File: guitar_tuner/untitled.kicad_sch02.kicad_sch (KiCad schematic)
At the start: 3 parts, among them Q2 NPN

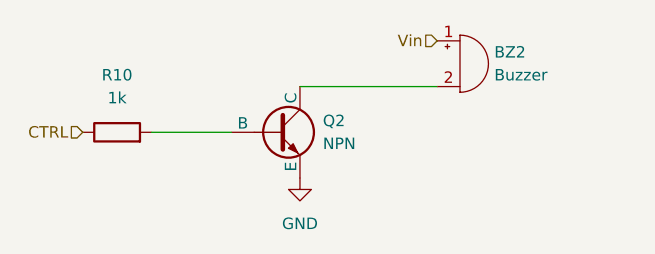
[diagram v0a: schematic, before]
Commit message: Buzzer Circuit Footprints and New Diode
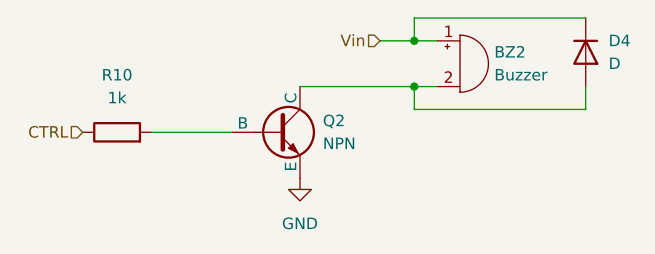
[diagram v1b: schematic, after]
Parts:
- added D4: D, Diode_SMD:D_0805_2012Metric_Pad1.15x1.40mm_HandSolder, symbol Device:D
- BZ2: footprint (none) -> Buzzer_Beeper:Buzzer_12x9.5RM7.6
- Q2: footprint (none) -> Package_TO_SOT_SMD:SOT-23_Handsoldering
- R10: footprint (none) -> Resistor_SMD:R_0805_2012Metric_Pad1.20x1.40mm_HandSolder
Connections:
- net Vin: now also D4.1 (K)
- net at BZ2.2 (-), Q2.1 (C): now also D4.2 (A)
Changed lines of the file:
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@@
 	(generator_version "9.0")
 	(paper "A4")
+	(junction
+		(at 157.48 99.06)
+		(diameter 0)
+		(color 0 0 0 0)
+	)
+	(junction
+		(at 157.48 93.98)
+		(diameter 0)
+		(color 0 0 0 0)
+	)
+	(wire
+		(pts
+			(xy 157.48 99.06) (xy 160.02 99.06)
+		)
+		(stroke
+			(width 0)
+			(type default)
+		)
+	)
+	(wire
+		(pts
+			(xy 176.53 101.6) (xy 176.53 99.06)
+		)
+		(stroke
+			(width 0)
+			(type default)
+		)
+	)
+	(wire
+		(pts
+			(xy 157.48 93.98) (xy 160.02 93.98)
+		)
+		(stroke
+			(width 0)
+			(type default)
+		)
+	)
 	(wire
 		(pts
@@
 	(wire
 		(pts
-			(xy 144.78 99.06) (xy 160.02 99.06)
+			(xy 144.78 99.06) (xy 157.48 99.06)
+		)
+		(stroke
+			(width 0)
+			(type default)
+		)
+	)
+	(wire
+		(pts
+			(xy 157.48 93.98) (xy 157.48 91.44)
+		)
+		(stroke
+			(width 0)
+			(type default)
+		)
+	)
+	(wire
+		(pts
+			(xy 157.48 101.6) (xy 176.53 101.6)
+		)
+		(stroke
+			(width 0)
+			(type default)
+		)
+	)
+	(wire
+		(pts
+			(xy 157.48 91.44) (xy 176.53 91.44)
+		)
+		(stroke
+			(width 0)
+			(type default)
+		)
+	)
+	(wire
+		(pts
+			(xy 153.67 93.98) (xy 157.48 93.98)
+		)
+		(stroke
+			(width 0)
+			(type default)
+		)
+	)
+	(wire
+		(pts
+			(xy 157.48 99.06) (xy 157.48 101.6)
 		)
 		(stroke
@@
 	(hierarchical_label "Vin"
 		(shape input)
-		(at 160.02 93.98 180)
+		(at 153.67 93.98 180)
 		(effects
 			(font
@@
 			)
 			(justify right)
+		)
+	)
+	(symbol
+		(lib_id "Device:D")
+		(at 176.53 95.25 270)
+		(unit 1)
+		(exclude_from_sim no)
+		(in_bom yes)
+		(on_board yes)
+		(dnp no)
+		(fields_autoplaced yes)
+		(property "Reference" "D4"
+			(at 179.07 93.9799 90)
+			(effects
+				(font
+					(size 1.27 1.27)
+				)
+				(justify left)
+			)
+		)
+		(property "Value" "D"
+			(at 179.07 96.5199 90)
+			(effects
+				(font
+					(size 1.27 1.27)
+				)
+				(justify left)
+			)
+		)
+		(property "Footprint" "Diode_SMD:D_0805_2012Metric_Pad1.15x1.40mm_HandSolder"
+			(at 176.53 95.25 0)
+			(effects
+				(font
+					(size 1.27 1.27)
+				)
+				(hide yes)
+			)
+		)
+		(property "Datasheet" "~"
+			(at 176.53 95.25 0)
+			(effects
+				(font
+					(size 1.27 1.27)
+				)
+				(hide yes)
+			)
+		)
+		(property "Description" "Diode"
+			(at 176.53 95.25 0)
+			(effects
+				(font
+					(size 1.27 1.27)
+				)
+				(hide yes)
+			)
+		)
+		(property "Sim.Device" "D"
+			(at 176.53 95.25 0)
+			(effects
+				(font
+					(size 1.27 1.27)
+				)
+				(hide yes)
+			)
+		)
+		(property "Sim.Pins" "1=K 2=A"
+			(at 176.53 95.25 0)
+			(effects
+				(font
+					(size 1.27 1.27)
+				)
+				(hide yes)
+			)
+		)
+		(pin "2"
+		)
+		(pin "1"
+		)
+		(instances
+			(project ""
+				(path "/66cd80e7-aa2b-4408-b572-7f7169004942/991b52bb-6157-43c3-ad9b-1fd2084c4c12"
+					(reference "D4")
+					(unit 1)
+				)
+			)
 		)
 	)
@@
 			)
 		)
-		(property "Footprint" ""
+		(property "Footprint" "Package_TO_SOT_SMD:SOT-23_Handsoldering"
 			(at 205.74 104.14 0)
 			(effects
@@
 			)
 		)
-		(property "Footprint" ""
+		(property "Footprint" "Buzzer_Beeper:Buzzer_12x9.5RM7.6"
 			(at 161.925 93.98 90)
 			(effects
@@
 			)
 		)
-		(property "Footprint" ""
+		(property "Footprint" "Resistor_SMD:R_0805_2012Metric_Pad1.20x1.40mm_HandSolder"
 			(at 124.46 105.918 90)
 			(effects

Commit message: Fixed ERC issue with buzzer circuit
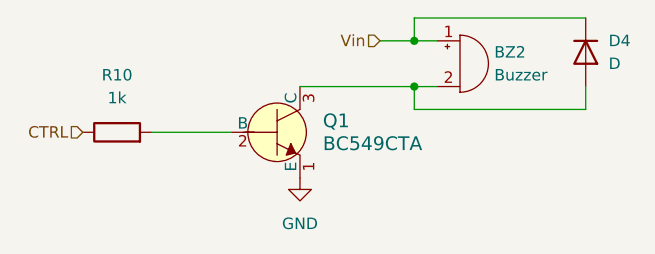
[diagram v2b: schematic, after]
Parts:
- removed Q2: NPN, Package_TO_SOT_SMD:SOT-23_Handsoldering, symbol Simulation_SPICE:NPN
- added Q1: BC549CTA, Package_TO_SOT_SMD:SOT-23_Handsoldering, symbol dk_Transistors-Bipolar-BJT-Single:BC549CTA
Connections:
- net GND: now also Q1.1 (E)
- net at BZ2.2 (-), D4.2 (A): now also Q1.3 (C)
- net at R10.2: now also Q1.2 (B)
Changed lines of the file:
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@@
-	)
-	(symbol
-		(lib_id "Simulation_SPICE:NPN")
-		(at 142.24 104.14 0)
-		(unit 1)
-		(exclude_from_sim no)
-		(in_bom yes)
-		(on_board yes)
-		(dnp no)
-		(fields_autoplaced yes)
-		(property "Reference" "Q2"
-			(at 147.32 102.8699 0)
-			(effects
-				(font
-					(size 1.27 1.27)
-				)
-				(justify left)
-			)
-		)
-		(property "Value" "NPN"
-			(at 147.32 105.4099 0)
-			(effects
-				(font
-					(size 1.27 1.27)
-				)
-				(justify left)
-			)
-		)
-		(property "Footprint" "Package_TO_SOT_SMD:SOT-23_Handsoldering"
-			(at 205.74 104.14 0)
-			(effects
-				(font
-					(size 1.27 1.27)
-				)
-				(hide yes)
-			)
-		)
-		(property "Datasheet" "https://ngspice.sourceforge.io/docs/ngspice-html-manual/manual.xhtml#cha_BJTs"
-			(at 205.74 104.14 0)
-			(effects
-				(font
-					(size 1.27 1.27)
-				)
-				(hide yes)
-			)
-		)
-		(property "Description" "Bipolar transistor symbol for simulation only, substrate tied to the emitter"
-			(at 142.24 104.14 0)
-			(effects
-				(font
-					(size 1.27 1.27)
-				)
-				(hide yes)
-			)
-		)
-		(property "Sim.Device" "NPN"
-			(at 142.24 104.14 0)
-			(effects
-				(font
-					(size 1.27 1.27)
-				)
-				(hide yes)
-			)
-		)
-		(property "Sim.Type" "GUMMELPOON"
-			(at 142.24 104.14 0)
-			(effects
-				(font
-					(size 1.27 1.27)
-				)
-				(hide yes)
-			)
-		)
-		(property "Sim.Pins" "1=C 2=B 3=E"
-			(at 142.24 104.14 0)
-			(effects
-				(font
-					(size 1.27 1.27)
-				)
-				(hide yes)
-			)
-		)
-		(pin "2"
-		)
-		(pin "3"
-		)
-		(pin "1"
-		)
-		(instances
-			(project "guitar_tuner"
-				(path "/66cd80e7-aa2b-4408-b572-7f7169004942/991b52bb-6157-43c3-ad9b-1fd2084c4c12"
-					(reference "Q2")
-					(unit 1)
-				)
-			)
-		)
 	)
 	(symbol
@@
 					(unit 1)
 				)
+			)
+		)
+	)
+	(symbol
+		(lib_id "dk_Transistors-Bipolar-BJT-Single:BC549CTA")
+		(at 142.24 104.14 0)
+		(unit 1)
+		(exclude_from_sim no)
+		(in_bom yes)
+		(on_board yes)
+		(dnp no)
+		(fields_autoplaced yes)
+		(property "Reference" "Q1"
+			(at 147.32 102.8699 0)
+			(effects
+				(font
+					(size 1.524 1.524)
+				)
+				(justify left)
+			)
+		)
+		(property "Value" "BC549CTA"
+			(at 147.32 105.4099 0)
+			(effects
+				(font
+					(size 1.524 1.524)
+				)
+				(justify left)
+			)
+		)
+		(property "Footprint" "Package_TO_SOT_SMD:SOT-23_Handsoldering"
+			(at 147.32 99.06 0)
+			(effects
+				(font
+					(size 1.524 1.524)
+				)
+				(justify left)
+				(hide yes)
+			)
+		)
+		(property "Datasheet" "https://www.onsemi.com/pub/Collateral/BC550-D.pdf"
+			(at 147.32 96.52 0)
+			(effects
+				(font
+					(size 1.524 1.524)
+				)
+				(justify left)
+				(hide yes)
+			)
+		)
+		(property "Description" "TRANS NPN 30V 0.1A TO-92"
+			(at 142.24 104.14 0)
+			(effects
+				(font
+					(size 1.27 1.27)
+				)
+				(hide yes)
+			)
+		)
+		(property "Digi-Key_PN" "BC549CTAFSCT-ND"
+			(at 147.32 93.98 0)
+			(effects
+				(font
+					(size 1.524 1.524)
+				)
+				(justify left)
+				(hide yes)
+			)
+		)
+		(property "MPN" "BC549CTA"
+			(at 147.32 91.44 0)
+			(effects
+				(font
+					(size 1.524 1.524)
+				)
+				(justify left)
+				(hide yes)
+			)
+		)
+		(property "Category" "Discrete Semiconductor Products"
+			(at 147.32 88.9 0)
+			(effects
+				(font
+					(size 1.524 1.524)
+				)
+				(justify left)
+				(hide yes)
+			)
+		)
+		(property "Family" "Transistors - Bipolar (BJT) - Single"
+			(at 147.32 86.36 0)
+			(effects
+				(font
+					(size 1.524 1.524)
+				)
+				(justify left)
+				(hide yes)
+			)
+		)
+		(property "DK_Datasheet_Link" "https://www.onsemi.com/pub/Collateral/BC550-D.pdf"
+			(at 147.32 83.82 0)
+			(effects
+				(font
+					(size 1.524 1.524)
+				)
+				(justify left)
+				(hide yes)
+			)
+		)
+		(property "DK_Detail_Page" "/product-detail/en/on-semiconductor/BC549CTA/BC549CTAFSCT-ND/3478139"
+			(at 147.32 81.28 0)
+			(effects
+				(font
+					(size 1.524 1.524)
+				)
+				(justify left)
+				(hide yes)
+			)
+		)
+		(property "Description_1" "TRANS NPN 30V 0.1A TO-92"
+			(at 147.32 78.74 0)
+			(effects
+				(font
+					(size 1.524 1.524)
+				)
+				(justify left)
+				(hide yes)
+			)
+		)
+		(property "Manufacturer" "ON Semiconductor"
+			(at 147.32 76.2 0)
+			(effects
+				(font
+					(size 1.524 1.524)
+				)
+				(justify left)
+				(hide yes)
+			)
+		)
+		(property "Status" "Active"
+			(at 147.32 73.66 0)
+			(effects
+				(font
+					(size 1.524 1.524)
+				)
+				(justify left)
+				(hide yes)
+			)
+		)
+		(pin "3"
+		)
+		(pin "2"
+		)
+		(pin "1"
+		)
+		(instances
+			(project ""
+				(path "/66cd80e7-aa2b-4408-b572-7f7169004942/991b52bb-6157-43c3-ad9b-1fd2084c4c12"
+					(reference "Q1")
+					(unit 1)
+				)
